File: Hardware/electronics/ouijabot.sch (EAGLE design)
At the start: 3 parts, among them J1 RASPBERRYPI-40-PIN-GPIO_PTH_N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

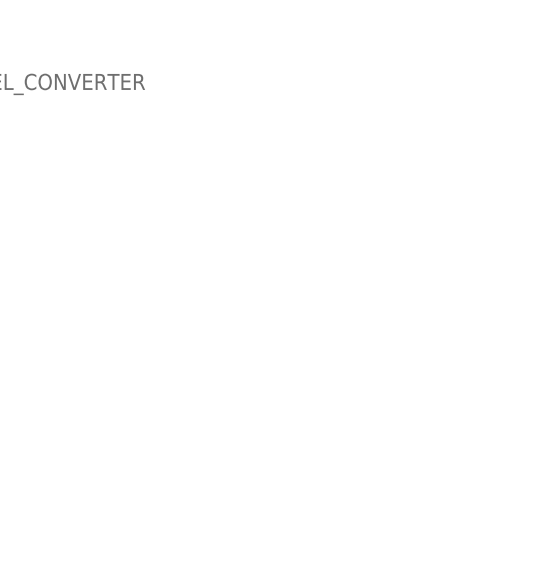
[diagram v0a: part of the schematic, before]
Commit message: Added ADC to schematic.
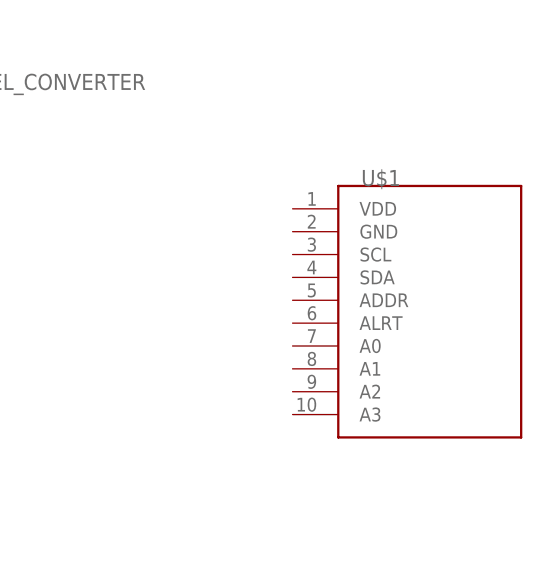
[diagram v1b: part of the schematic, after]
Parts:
- added U$1: (no value), ouijabot:ADS1115
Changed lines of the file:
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@@
 <setting verticaltext="up"/>
 </settings>
-<grid distance="0.1" unitdist="inch" unit="inch" style="lines" multiple="1" display="no" altdistance="0.01" altunitdist="inch" altunit="inch"/>
+<grid distance="0.1" unitdist="inch" unit="inch" style="lines" multiple="1" display="yes" altdistance="0.01" altunitdist="inch" altunit="inch"/>
 <layers>
 <layer number="1" name="Top" color="4" fill="1" visible="no" active="no"/>
+<layer number="2" name="Route2" color="16" fill="1" visible="no" active="no"/>
+<layer number="3" name="Route3" color="17" fill="1" visible="no" active="no"/>
+<layer number="4" name="Route4" color="18" fill="1" visible="no" active="no"/>
+<layer number="5" name="Route5" color="19" fill="1" visible="no" active="no"/>
+<layer number="6" name="Route6" color="25" fill="1" visible="no" active="no"/>
+<layer number="7" name="Route7" color="26" fill="1" visible="no" active="no"/>
+<layer number="8" name="Route8" color="27" fill="1" visible="no" active="no"/>
+<layer number="9" name="Route9" color="28" fill="1" visible="no" active="no"/>
+<layer number="10" name="Route10" color="29" fill="1" visible="no" active="no"/>
+<layer number="11" name="Route11" color="30" fill="1" visible="no" active="no"/>
+<layer number="12" name="Route12" color="20" fill="1" visible="no" active="no"/>
+<layer number="13" name="Route13" color="21" fill="1" visible="no" active="no"/>
+<layer number="14" name="Route14" color="22" fill="1" visible="no" active="no"/>
+<layer number="15" name="Route15" color="23" fill="1" visible="no" active="no"/>
 <layer number="16" name="Bottom" color="1" fill="1" visible="no" active="no"/>
 <layer number="17" name="Pads" color="2" fill="1" visible="no" active="no"/>
@@
 <part name="B1" library="SparkFun-Boards" deviceset="SPARKFUN_LOGIC_LEVEL_CONVERTER" device=""/>
 <part name="B2" library="SparkFun-Boards" deviceset="SPARKFUN_LOGIC_LEVEL_CONVERTER" device=""/>
+<part name="U$1" library="ouijabot" deviceset="ADS1115" device=""/>
 </parts>
 <sheets>
@@
 <attribute name="VALUE" x="91.44" y="60.706" size="1.778" layer="95" font="vector" align="top-left"/>
 </instance>
+<instance part="U$1" gate="G$1" x="157.48" y="33.02" smashed="yes">
+<attribute name="NAME" x="157.48" y="48.26" size="1.778" layer="95"/>
+<attribute name="VALUE" x="162.56" y="2.54" size="1.778" layer="96"/>
+</instance>
 </instances>
 <busses>
@@
 </schematic>
 </drawing>
+<compatibility>
+<note version="8.3" severity="warning">
+Since Version 8.3, EAGLE supports URNs for individual library
+assets (packages, symbols, and devices). The URNs of those assets
+will not be understood (or retained) with this version.
+</note>
+</compatibility>
 </eagle>

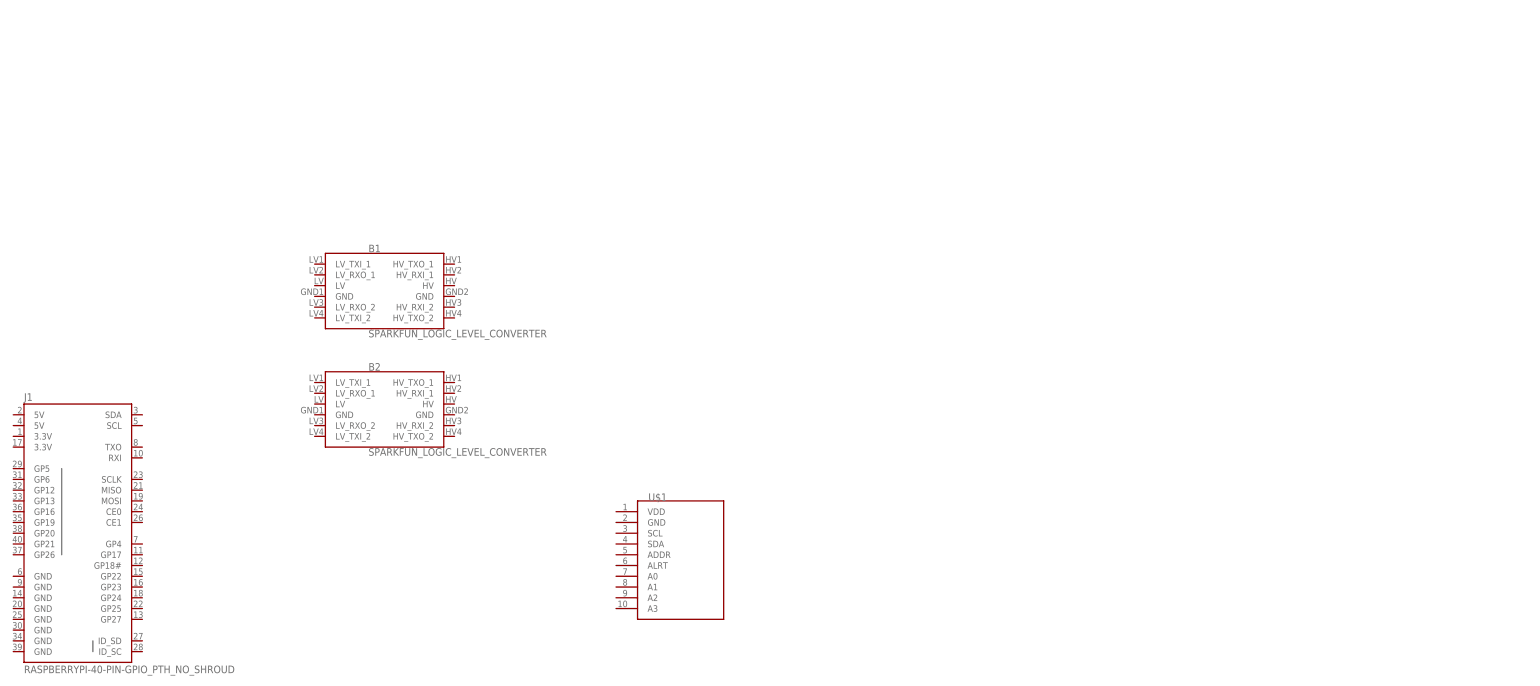
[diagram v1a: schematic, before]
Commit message: Finished adding parts to library.
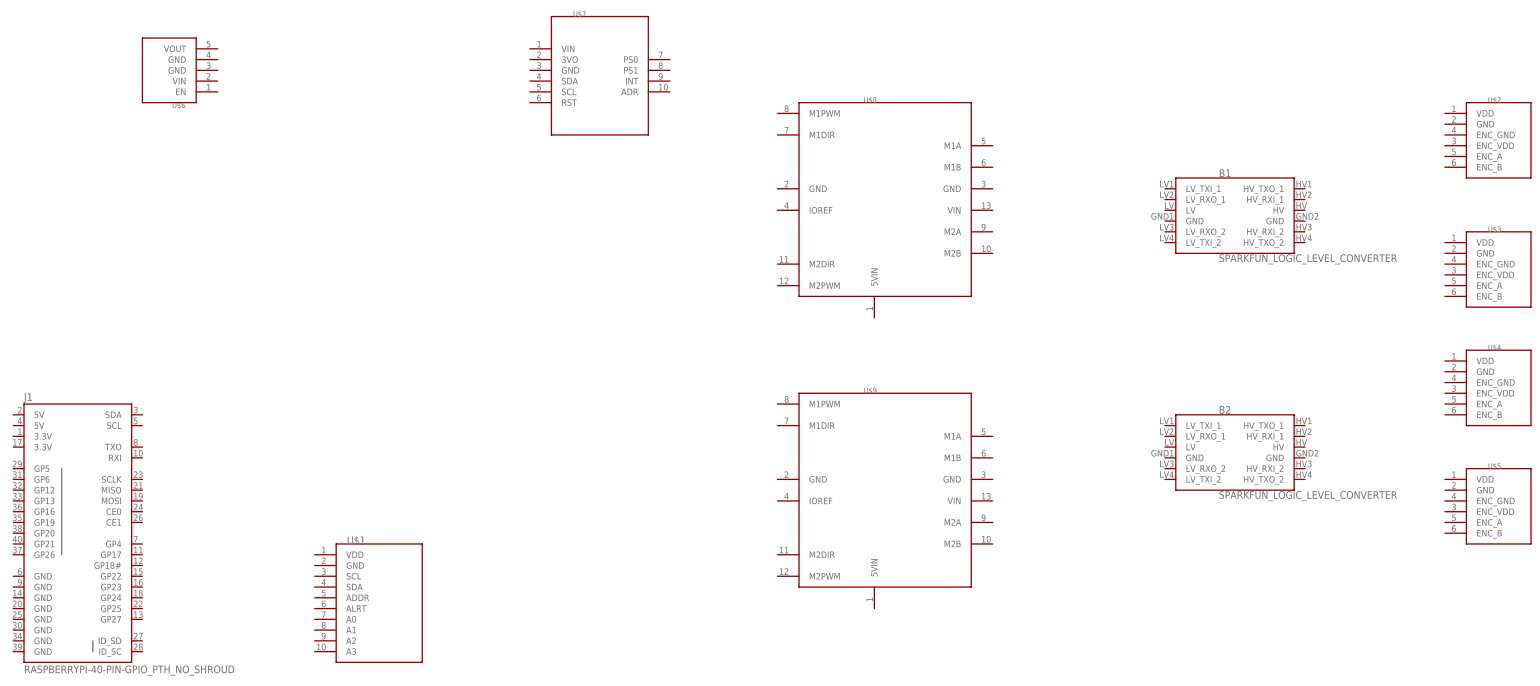
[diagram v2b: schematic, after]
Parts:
- added U$2, U$3, U$4, U$5: (no value), ouijabot:P2823
- added U$6: (no value), ouijabot:P2851
- added U$7: (no value), ouijabot:BNO055
- added U$8, U$9: (no value), ouijabot:TB9051FTG
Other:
- moved on the sheet: B1, B2, U$1
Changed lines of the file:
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@@
 <setting verticaltext="up"/>
 </settings>
-<grid distance="0.1" unitdist="inch" unit="inch" style="lines" multiple="1" display="yes" altdistance="0.01" altunitdist="inch" altunit="inch"/>
+<grid distance="0.1" unitdist="inch" unit="inch" style="lines" multiple="1" display="no" altdistance="0.01" altunitdist="inch" altunit="inch"/>
 <layers>
 <layer number="1" name="Top" color="4" fill="1" visible="no" active="no"/>
@@
 <part name="B2" library="SparkFun-Boards" deviceset="SPARKFUN_LOGIC_LEVEL_CONVERTER" device=""/>
 <part name="U$1" library="ouijabot" deviceset="ADS1115" device=""/>
+<part name="U$2" library="ouijabot" deviceset="P2823" device=""/>
+<part name="U$3" library="ouijabot" deviceset="P2823" device=""/>
+<part name="U$4" library="ouijabot" deviceset="P2823" device=""/>
+<part name="U$5" library="ouijabot" deviceset="P2823" device=""/>
+<part name="U$6" library="ouijabot" deviceset="P2851" device=""/>
+<part name="U$7" library="ouijabot" deviceset="BNO055" device=""/>
+<part name="U$8" library="ouijabot" deviceset="TB9051FTG" device=""/>
+<part name="U$9" library="ouijabot" deviceset="TB9051FTG" device=""/>
 </parts>
 <sheets>
@@
 <attribute name="VALUE" x="10.16" y="7.62" size="1.778" layer="96"/>
 </instance>
-<instance part="B1" gate="G$1" x="96.52" y="96.52" smashed="yes">
-<attribute name="NAME" x="91.44" y="106.934" size="1.778" layer="95" font="vector"/>
-<attribute name="VALUE" x="91.44" y="88.646" size="1.778" layer="95" font="vector" align="top-left"/>
-</instance>
-<instance part="B2" gate="G$1" x="96.52" y="68.58" smashed="yes">
-<attribute name="NAME" x="91.44" y="78.994" size="1.778" layer="95" font="vector"/>
-<attribute name="VALUE" x="91.44" y="60.706" size="1.778" layer="95" font="vector" align="top-left"/>
-</instance>
-<instance part="U$1" gate="G$1" x="157.48" y="33.02" smashed="yes">
-<attribute name="NAME" x="157.48" y="48.26" size="1.778" layer="95"/>
-<attribute name="VALUE" x="162.56" y="2.54" size="1.778" layer="96"/>
+<instance part="B1" gate="G$1" x="297.18" y="114.3" smashed="yes">
+<attribute name="NAME" x="292.1" y="124.714" size="1.778" layer="95" font="vector"/>
+<attribute name="VALUE" x="292.1" y="106.426" size="1.778" layer="95" font="vector" align="top-left"/>
+</instance>
+<instance part="B2" gate="G$1" x="297.18" y="58.42" smashed="yes">
+<attribute name="NAME" x="292.1" y="68.834" size="1.778" layer="95" font="vector"/>
+<attribute name="VALUE" x="292.1" y="50.546" size="1.778" layer="95" font="vector" align="top-left"/>
+</instance>
+<instance part="U$1" gate="G$1" x="86.36" y="22.86" smashed="yes">
+<attribute name="NAME" x="86.36" y="38.1" size="1.778" layer="95"/>
+<attribute name="VALUE" x="91.44" y="-7.62" size="1.778" layer="96"/>
+</instance>
+<instance part="U$2" gate="G$1" x="355.6" y="134.62" smashed="yes">
+<attribute name="NAME" x="355.6" y="142.24" size="1.27" layer="95"/>
+<attribute name="VALUE" x="355.6" y="121.92" size="1.27" layer="96"/>
+</instance>
+<instance part="U$3" gate="G$1" x="355.6" y="104.14" smashed="yes">
+<attribute name="NAME" x="355.6" y="111.76" size="1.27" layer="95"/>
+<attribute name="VALUE" x="355.6" y="91.44" size="1.27" layer="96"/>
+</instance>
+<instance part="U$4" gate="G$1" x="355.6" y="76.2" smashed="yes">
+<attribute name="NAME" x="355.6" y="83.82" size="1.27" layer="95"/>
+<attribute name="VALUE" x="355.6" y="63.5" size="1.27" layer="96"/>
+</instance>
+<instance part="U$5" gate="G$1" x="355.6" y="48.26" smashed="yes">
+<attribute name="NAME" x="355.6" y="55.88" size="1.27" layer="95"/>
+<attribute name="VALUE" x="355.6" y="35.56" size="1.27" layer="96"/>
+</instance>
+<instance part="U$6" gate="G$1" x="48.26" y="149.86" smashed="yes" rot="R180">
+<attribute name="NAME" x="48.26" y="142.24" size="1.27" layer="95" rot="R180"/>
+<attribute name="VALUE" x="48.26" y="160.02" size="1.27" layer="95" rot="R180"/>
+</instance>
+<instance part="U$7" gate="G$1" x="137.16" y="152.4" smashed="yes">
+<attribute name="NAME" x="139.7" y="162.56" size="1.27" layer="95"/>
+<attribute name="VALUE" x="139.7" y="142.24" size="1.27" layer="96"/>
+</instance>
+<instance part="U$8" gate="G$1" x="200.66" y="119.38" smashed="yes">
+<attribute name="NAME" x="208.28" y="142.24" size="1.27" layer="95"/>
+<attribute name="VALUE" x="213.36" y="93.98" size="1.27" layer="96"/>
+</instance>
+<instance part="U$9" gate="G$1" x="200.66" y="50.8" smashed="yes">
+<attribute name="NAME" x="208.28" y="73.66" size="1.27" layer="95"/>
+<attribute name="VALUE" x="213.36" y="25.4" size="1.27" layer="96"/>
 </instance>
 </instances>
